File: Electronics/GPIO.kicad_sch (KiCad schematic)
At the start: 30 parts, among them J10 Conn_01x02, J11 JST_SHBM04B-SRSS-TB, J12 JST_SHBM04B-SRSS-TB, J3 RJ45_RB1-125B8G1A, J4 Conn_01x07, J5 Micro_SD_Card_Det, J6 Conn_01x04, J7 Conn_02x07_Odd_Even, J8 JST_SHBM04B-SRSS-TB, J9 JST_SHBM04B-SRSS-TB, Q1 BSS84AKW115, U2 TPD4EUSB30, U3 TPD4EUSB30, U4 74LVC1G07SE-7, U5 RT9742GGJ5

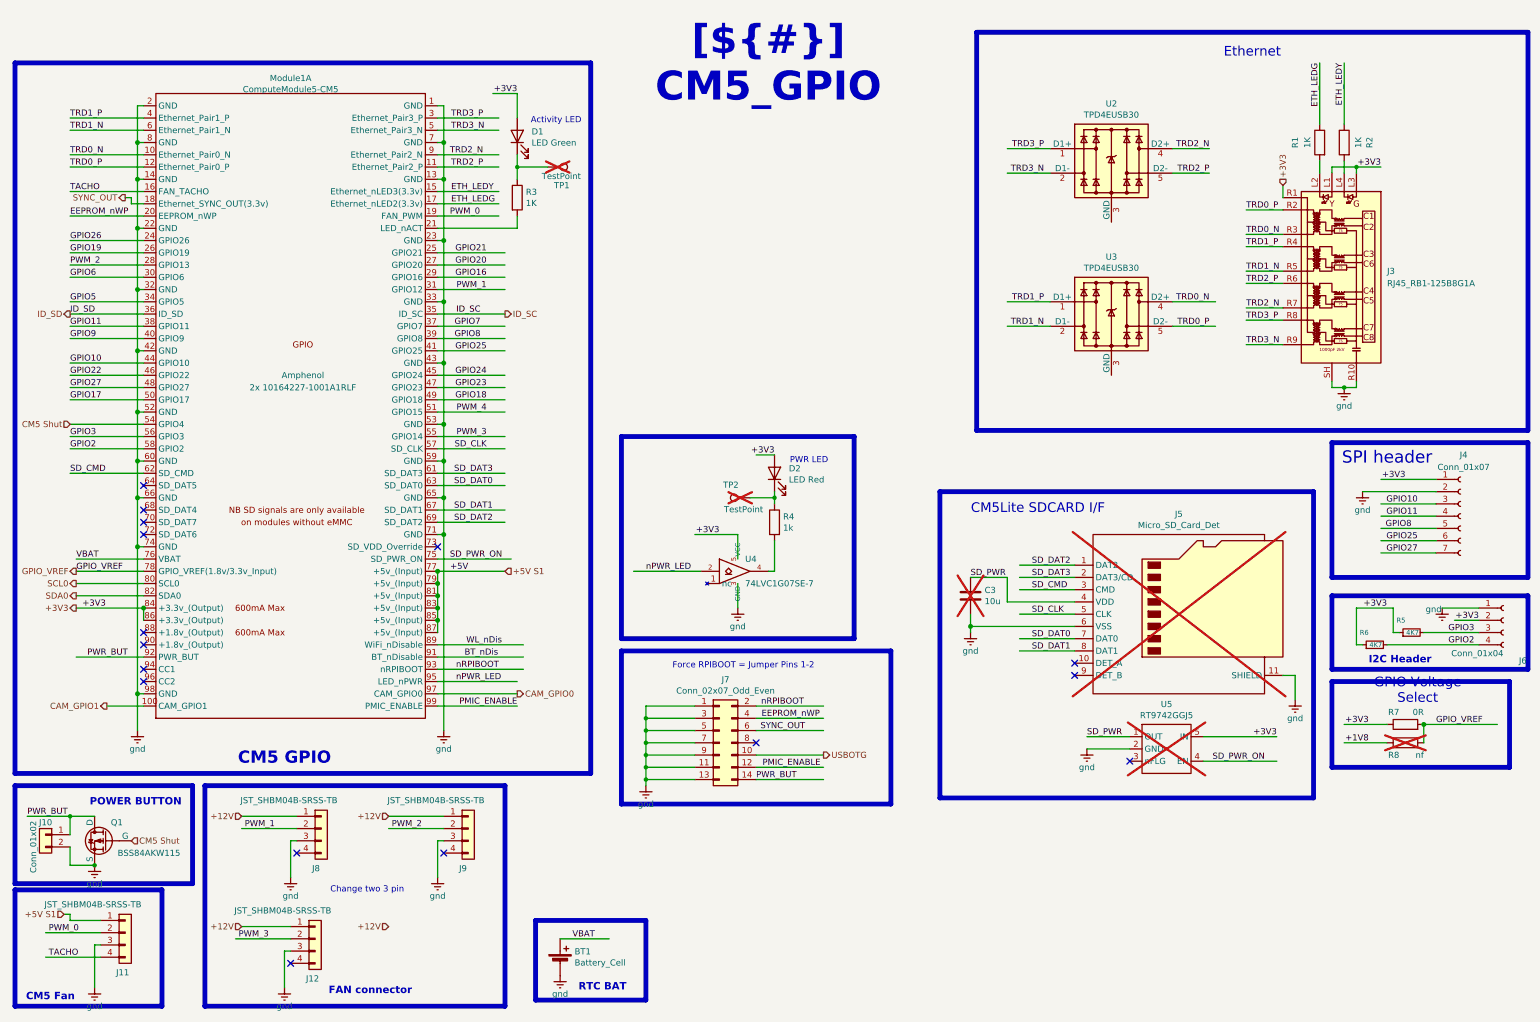
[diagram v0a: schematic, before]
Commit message: Power symbols changed and sata hub fixed schem
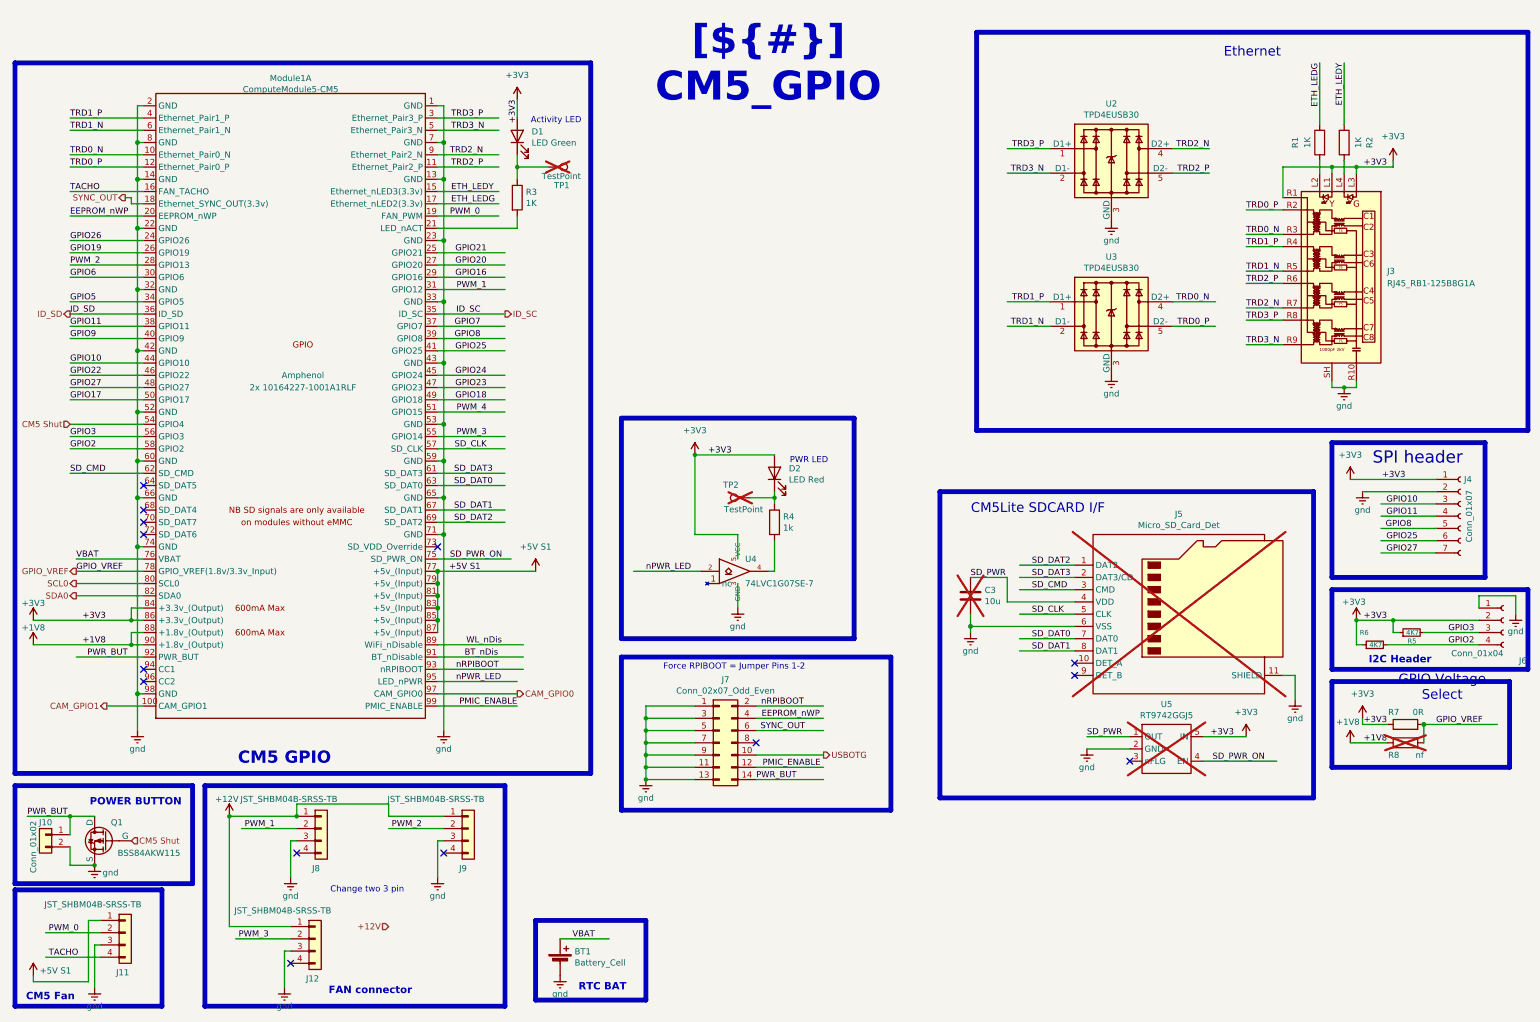
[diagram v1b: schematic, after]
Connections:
- net +1V8: now also Module1.88 (+1.8v_(Output)), Module1.90 (+1.8v_(Output))
- net gnd: now also U2.3 (GND), U2.8 (GND), U3.3 (GND), U3.8 (GND)
- no-connect marks 16 -> 14

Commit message: Fans
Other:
- note added: "Change two 0470531000 add tacho"
- note removed: "Change two 3 pin"
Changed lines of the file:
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@@
 		)
 	)
-	(text "Change two 3 pin"
+	(text "Change two 0470531000\nadd tacho\n"
 		(exclude_from_sim no)
 		(at 86.995 191.77 0)
@@
 		(polyline
 			(pts
-				(xy 306.07 110.49) (xy 306.07 123.19) (xy 308.61 123.19) (xy 308.61 110.49)
+				(xy 267.97 48.26) (xy 275.59 48.26) (xy 276.86 49.53) (xy 276.86 80.01) (xy 267.97 80.01)
 			)
 			(stroke
@@
 		(polyline
 			(pts
-				(xy 306.07 138.43) (xy 308.61 138.43) (xy 308.61 142.24) (xy 306.07 142.24)
+				(xy 35.56 127) (xy 38.1 127) (xy 38.1 132.08) (xy 35.56 132.08)
 			)
 			(stroke
@@
 		(polyline
 			(pts
-				(xy 35.56 127) (xy 38.1 127) (xy 38.1 132.08) (xy 35.56 132.08)
+				(xy 306.07 110.49) (xy 306.07 123.19) (xy 308.61 123.19) (xy 308.61 110.49)
 			)
 			(stroke
@@
 		(polyline
 			(pts
-				(xy 267.97 48.26) (xy 275.59 48.26) (xy 276.86 49.53) (xy 276.86 80.01) (xy 267.97 80.01)
+				(xy 306.07 138.43) (xy 308.61 138.43) (xy 308.61 142.24) (xy 306.07 142.24)
 			)
 			(stroke
